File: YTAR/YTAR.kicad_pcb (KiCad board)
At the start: 6 copper layers, 50 x 50 mm, 148 parts, among them J1 STDC14, J2 CAMERA, J3 Micro_Sd, J5 USB_C_USB4085-GF-A, J6 IO, SW1 Tact, U1 STM32H750XBHx, U2 MCP2562-E-MF, U3 DS90C124, Y1 25MHz

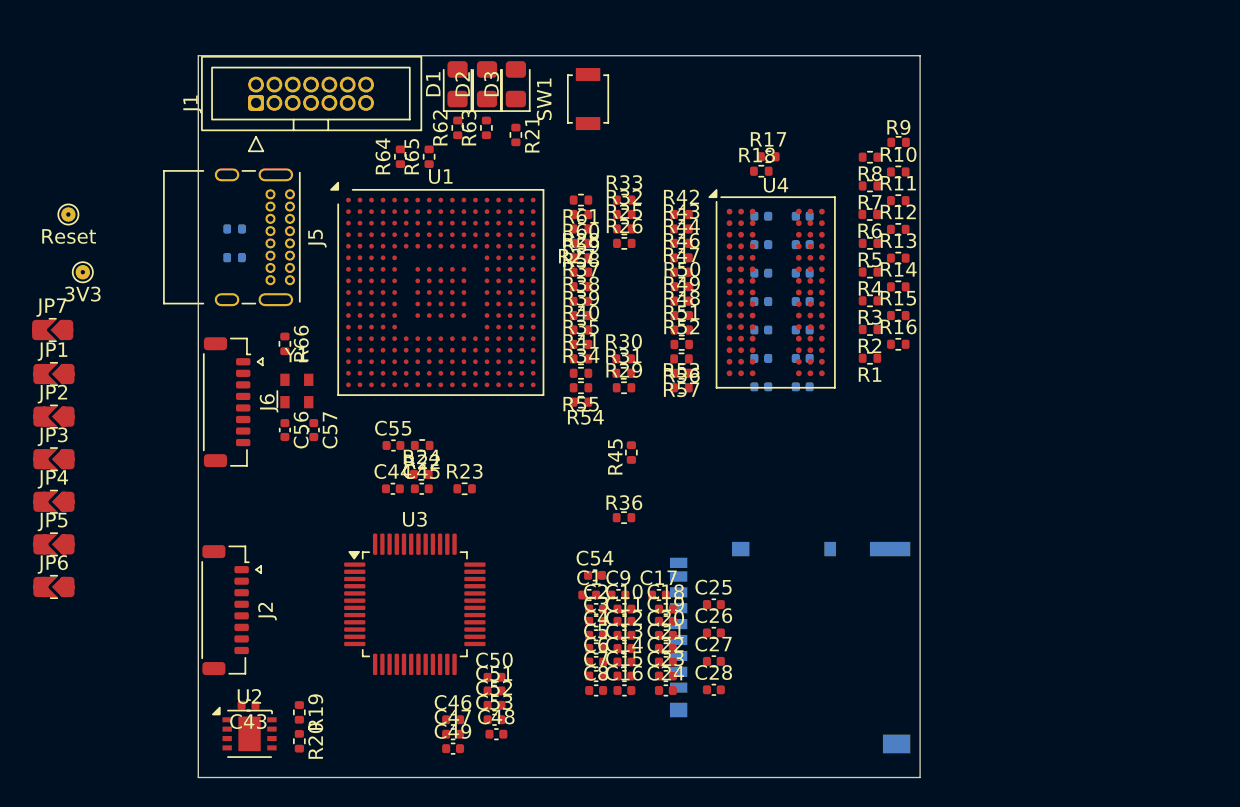
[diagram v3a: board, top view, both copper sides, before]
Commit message: Added LCD labels and corredted SRAM
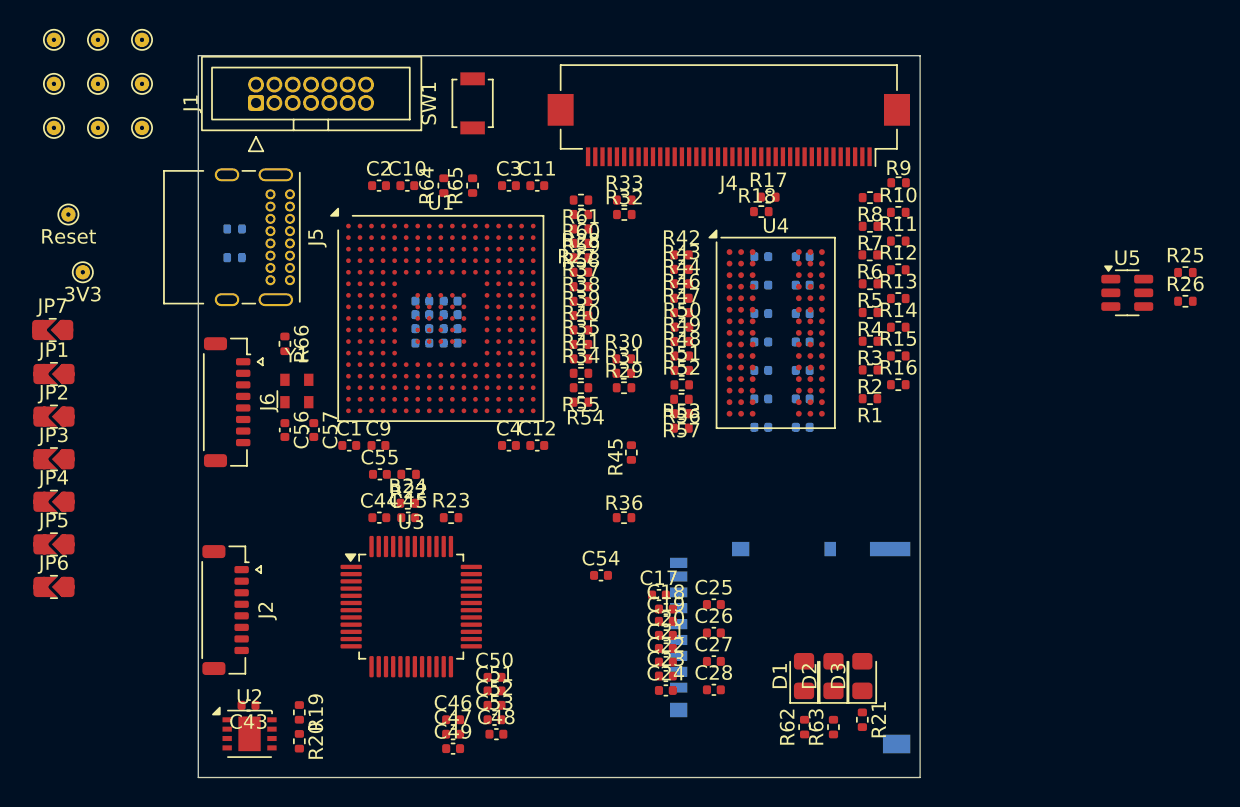
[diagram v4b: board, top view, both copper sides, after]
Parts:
- added J4: FH12-40S-0.5SH(55), Connector_FFC-FPC:Hirose_FH12-40S-0.5SH_1x40-1MP_P0.50mm_Horizontal, F.Cu at (48.8, 17.1)
- added TP10: ~, MEMS_Custom:TestPoint_Pad_D1.0mm, F.Cu at (8.10, 13.9)
- added TP11: ~, MEMS_Custom:TestPoint_Pad_D1.0mm, F.Cu at (8.10, 17.0)
- added TP3: ~, MEMS_Custom:TestPoint_Pad_D1.0mm, F.Cu at (2.00, 10.9)
- added TP4: ~, MEMS_Custom:TestPoint_Pad_D1.0mm, F.Cu at (2.00, 13.9)
- added TP5: ~, MEMS_Custom:TestPoint_Pad_D1.0mm, F.Cu at (2.00, 17.0)
- added TP6: ~, MEMS_Custom:TestPoint_Pad_D1.0mm, F.Cu at (5.05, 10.9)
- added TP7: ~, MEMS_Custom:TestPoint_Pad_D1.0mm, F.Cu at (5.05, 13.9)
- added TP8: ~, MEMS_Custom:TestPoint_Pad_D1.0mm, F.Cu at (5.05, 17.0)
- added TP9: ~, MEMS_Custom:TestPoint_Pad_D1.0mm, F.Cu at (8.10, 10.9)
- added U5: TPS56339, Package_TO_SOT_SMD:TSOT-23-6, F.Cu at (76.3, 28.4)
- C13, C14, C15, C16, C5, C6, C7, C8: moved to B.Cu
- moved R63 48.0 mm to (56.0, 58.5)
- moved R62 48.0 mm to (54.0, 58.5)
- moved D1 47.5 mm to (54.0, 55.0)
- moved D2 47.5 mm to (56.0, 55.0)
- moved D3 47.5 mm to (58.0, 55.0)
- moved R21 47.1 mm to (58.0, 58.0)
- moved R26 39.1 mm to (80.4, 29.0)
- moved R25 39.0 mm to (80.4, 27.0)
- moved C10 33.0 mm to (26.5, 21.0)
- moved C2 33.0 mm to (24.5, 21.0)
- moved C11 30.8 mm to (35.5, 21.0)
- moved C3 30.8 mm to (33.5, 21.0)
- moved C13 27.8 mm to (27.5, 29.0), turned to 180 degrees
- moved C14 27.8 mm to (27.5, 29.9), turned to 180 degrees
- moved C15 27.8 mm to (27.5, 30.9), turned to 180 degrees
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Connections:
- C10 pad 1: +3.3V -> VDDA
- C11 pad 1: +3.3V -> VDDA
- C12 pad 1: +3.3V -> VDDA
- C13 pad 1: +3.3V -> VDDA
- C14 pad 1: +3.3V -> VDDA
- C15 pad 1: +3.3V -> VDDA
- C16 pad 1: +3.3V -> VDDA
- C17 pad 1: +3.3V -> VDDA
- C18 pad 1: +3.3V -> VDDA
- C19 pad 1: +3.3V -> VDDA
- C20 pad 1: +3.3V -> VDDA
- C21 pad 1: +3.3V -> VDDA
- C22 pad 1: +3.3V -> VDDA
- C23 pad 1: +3.3V -> VDDA
- C24 pad 1: +3.3V -> VDDA
- C3 pad 1: +3.3V -> VDDA
- C4 pad 1: +3.3V -> VDDA
- C5 pad 1: +3.3V -> VDDA
- C6 pad 1: +3.3V -> VDDA
- C7 pad 1: +3.3V -> VDDA
- C8 pad 1: +3.3V -> VDDA
- C9 pad 1: +3.3V -> VDDA
- J6 pad 1: unconnected-(J6-Pin_1-Pad1) -> +12V_IN
- J6 pad 2: unconnected-(J6-Pin_2-Pad2) -> GND
- R25 pad 1: Net-(U1-PC14) -> Net-(U1-PD14)
- R26 pad 1: Net-(U1-PC15) -> Net-(U1-PD15)
- U1 pad A13: unconnected-(U1-PC10-PadA13) -> /ROUT10
- U1 pad A15: unconnected-(U1-PI1-PadA15) -> /LCD_G6
- U1 pad A16: unconnected-(U1-PI0-PadA16) -> /LCD_G5
- U1 pad A8: unconnected-(U1-PK5-PadA8) -> /LCD_B6
- U1 pad B10: unconnected-(U1-PJ15-PadB10) -> /LCD_B3
- U1 pad B13: unconnected-(U1-PC11-PadB13) -> /ROUT11
- U1 pad B8: unconnected-(U1-PK4-PadB8) -> /LCD_B5
- U1 pad C1: Net-(U1-PC15) -> /ROUT15
- U1 pad C12: unconnected-(U1-PC12-PadC12) -> /ROUT12
- U1 pad C2: Net-(U1-PC14) -> /ROUT14
- U1 pad C7: unconnected-(U1-PK6-PadC7) -> /LCD_B7
- U1 pad C8: unconnected-(U1-PK3-PadC8) -> /LCD_B4
- U1 pad D10: unconnected-(U1-PJ14-PadD10) -> /LCD_B2
- U1 pad D11: unconnected-(U1-PJ12-PadD11) -> /LCD_B0
- U1 pad D7: unconnected-(U1-PK7-PadD7) -> /LCD_DE
- U1 pad E10: unconnected-(U1-PJ13-PadE10) -> /LCD_B1
- U1 pad E13: unconnected-(U1-PC8-PadE13) -> /ROUT8
- U1 pad E14: unconnected-(U1-PC9-PadE14) -> /ROUT9
- U1 pad E2: unconnected-(U1-PI9-PadE2) -> /LCD_VSYNC
- U1 pad E3: unconnected-(U1-PC13-PadE3) -> /ROUT13
- U1 pad F13: unconnected-(U1-PC7-PadF13) -> /ROUT7
- U1 pad F14: unconnected-(U1-PC6-PadF14) -> /ROUT6
- U1 pad H1: unconnected-(U1-PI12-PadH1) -> /LCD_HSYNC
- U1 pad H17: unconnected-(U1-PK2-PadH17) -> /LCD_G7
- U1 pad H3: unconnected-(U1-PI14-PadH3) -> /LCD_CLK
- U1 pad K14: unconnected-(U1-PJ11-PadK14) -> /LCD_G4
- U1 pad L14: unconnected-(U1-PJ10-PadL14) -> /LCD_G3
- U1 pad L2: unconnected-(U1-PC0-PadL2) -> /ROUT0
- U1 pad M14: unconnected-(U1-PJ9-PadM14) -> /LCD_G2
- U1 pad M2: unconnected-(U1-PC1-PadM2) -> /ROUT1
- U1 pad M3: unconnected-(U1-PC2-PadM3) -> /ROUT2
- U1 pad M4: unconnected-(U1-PC3-PadM4) -> /ROUT3
- U1 pad N13: unconnected-(U1-PJ8-PadN13) -> /LCD_G1
- U1 pad N14: unconnected-(U1-PJ7-PadN14) -> /LCD_G0
- U1 pad N15: unconnected-(U1-PJ6-PadN15) -> /LCD_R7
- U1 pad N6: unconnected-(U1-PJ0-PadN6) -> /LCD_R1
- U1 pad P15: unconnected-(U1-PD15-PadP15) -> Net-(U1-PD15)
- U1 pad P16: unconnected-(U1-PD14-PadP16) -> Net-(U1-PD14)
- U1 pad P5: unconnected-(U1-PI15-PadP5) -> /LCD_R0
- U1 pad P6: unconnected-(U1-PJ1-PadP6) -> /LCD_R2
- U1 pad R12: unconnected-(U1-PJ5-PadR12) -> /LCD_R6
- U1 pad R13: unconnected-(U1-PH9-PadR13) -> /LCD_R3
- U1 pad R16: unconnected-(U1-PD12-PadR16) -> /LCD_SCL
- U1 pad R17: unconnected-(U1-PD13-PadR17) -> /LCD_SDA
- U1 pad T4: unconnected-(U1-PC4-PadT4) -> /ROUT4
- U1 pad U4: unconnected-(U1-PC5-PadU4) -> /ROUT5
- U1 pad U6: unconnected-(U1-PJ3-PadU6) -> /LCD_R4
- U1 pad U7: unconnected-(U1-PJ4-PadU7) -> /LCD_R5

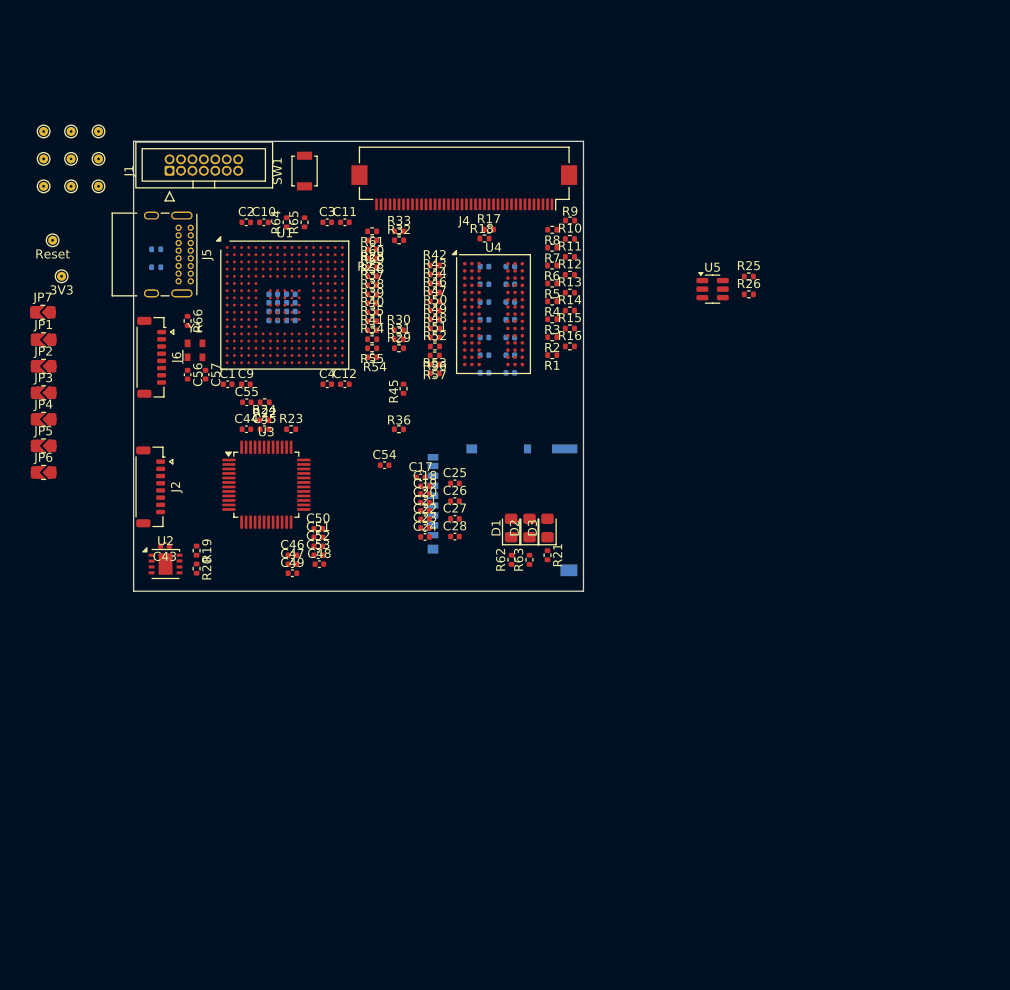
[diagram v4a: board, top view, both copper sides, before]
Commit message: Started a bit of routing
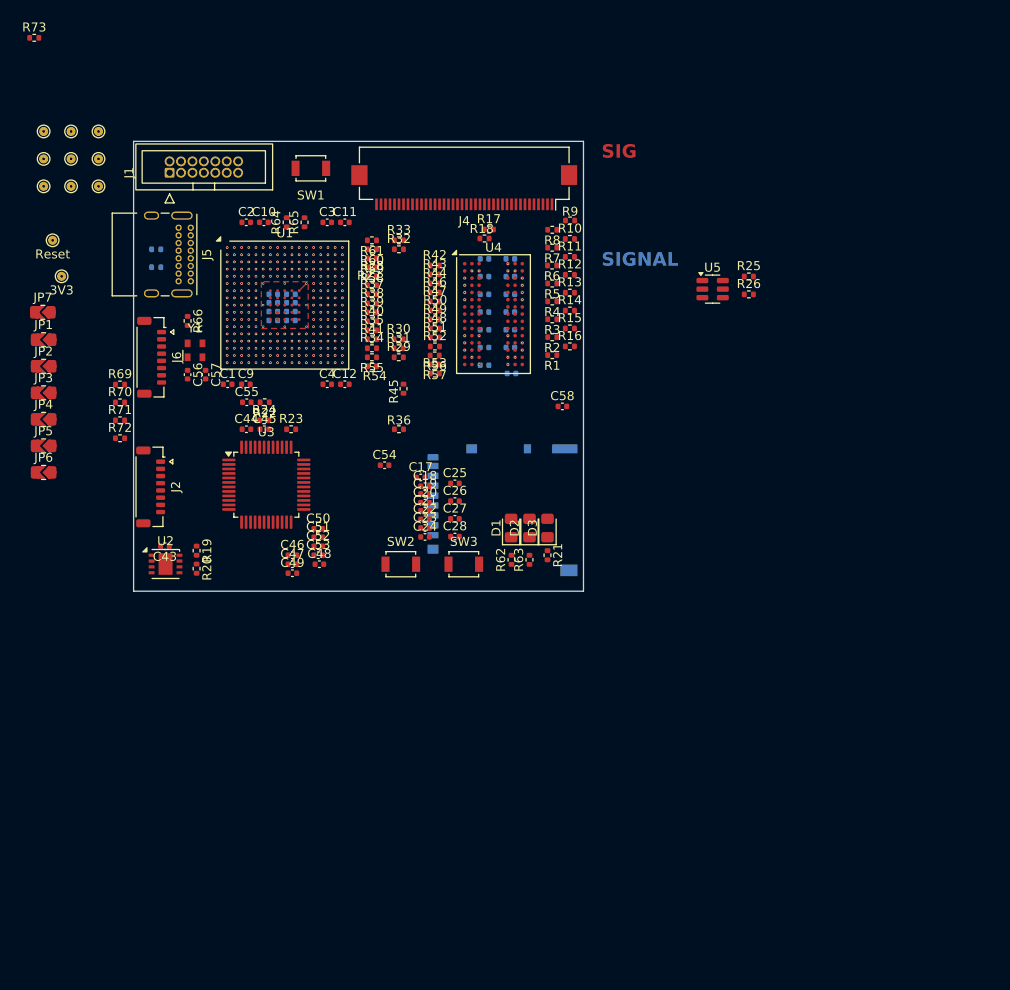
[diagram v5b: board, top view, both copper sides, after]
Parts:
- added C58: 2.2u, Capacitor_SMD:C_0402_1005Metric, F.Cu at (59.7, 41.5)
- added R69: 10k, Resistor_SMD:R_0402_1005Metric, F.Cu at (10.5, 39.0)
- added R70: 10k, Resistor_SMD:R_0402_1005Metric, F.Cu at (10.5, 41.0)
- added R71: 5k1, Resistor_SMD:R_0402_1005Metric, F.Cu at (10.5, 43.0)
- added R72: 5k1, Resistor_SMD:R_0402_1005Metric, F.Cu at (10.5, 45.0)
- added R73: 0R, Resistor_SMD:R_0402_1005Metric, F.Cu at (0.95, 0.49)
- added SW2: PICTURE, Button_Switch_SMD:SW_SPST_B3U-1000P, F.Cu at (41.7, 59.0)
- added SW3: MODE, Button_Switch_SMD:SW_SPST_B3U-1000P, F.Cu at (48.7, 59.0)
- SW1: value Tact -> RESET
- moved R29 1.00 mm to (41.5, 36.0)
- moved R27 1.00 mm to (38.5, 28.0)
- moved R28 1.00 mm to (38.5, 27.0)
- moved R30 1.00 mm to (41.5, 34.0)
- moved R31 1.00 mm to (41.5, 35.0)
- moved R32 1.00 mm to (41.5, 24.0)
- moved R33 1.00 mm to (41.5, 23.0)
- moved R34 1.00 mm to (38.5, 35.0)
- moved R35 1.00 mm to (38.5, 33.0)
- moved R37 1.00 mm to (38.5, 29.0)
- moved R38 1.00 mm to (38.5, 30.0)
- moved R39 1.00 mm to (38.5, 31.0)
- moved R40 1.00 mm to (38.5, 32.0)
- moved R41 1.00 mm to (38.5, 34.0)
- moved R54 1.00 mm to (38.5, 37.0)
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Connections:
- C10 pad 1: VDDA -> VDD_MCU
- C11 pad 1: VDDA -> VDD_MCU
- C12 pad 1: VDDA -> VDD_MCU
- C13 pad 1: VDDA -> VDD_MCU
- C14 pad 1: VDDA -> VDD_MCU
- C15 pad 1: VDDA -> VDD_MCU
- C16 pad 1: VDDA -> VDD_MCU
- C17 pad 1: VDDA -> VDD_MCU
- C18 pad 1: VDDA -> VDD_MCU
- C19 pad 1: VDDA -> VDD_MCU
- C20 pad 1: VDDA -> VDD_MCU
- C21 pad 1: VDDA -> VDD_MCU
- C22 pad 1: VDDA -> VDD_MCU
- C23 pad 1: VDDA -> VDD_MCU
- C24 pad 1: VDDA -> VDD_MCU
- C25 pad 1: VDDA -> VDD_MCU
- C26 pad 1: VDDA -> VDD_MCU
- C27 pad 1: VDDA -> VDD_MCU
- C3 pad 1: VDDA -> VDD_MCU
- C4 pad 1: VDDA -> VDD_MCU
- C5 pad 1: VDDA -> VDD_MCU
- C54 pad 1: VDDA -> VDD_MCU
- C6 pad 1: VDDA -> VDD_MCU
- C7 pad 1: VDDA -> VDD_MCU
- C8 pad 1: VDDA -> VDD_MCU
- C9 pad 1: VDDA -> VDD_MCU
- J1 pad 3: VDDA -> VDD_MCU
- J3 pad 1: unconnected-(J3-DAT2-Pad1) -> /SD_D2
- J3 pad 10: unconnected-(J3-DET_A-Pad10) -> /SD_DET_A
- J3 pad 11: unconnected-(J3-SHIELD-Pad11) -> GND
- J3 pad 2: unconnected-(J3-DAT3/CD-Pad2) -> /SD_D3
- J3 pad 3: unconnected-(J3-CMD-Pad3) -> /SD_CMD
- J3 pad 4: unconnected-(J3-VDD-Pad4) -> VDD_MCU
- J3 pad 5: unconnected-(J3-CLK-Pad5) -> /SD_CK
- J3 pad 6: unconnected-(J3-VSS-Pad6) -> GND
- J3 pad 7: unconnected-(J3-DAT0-Pad7) -> /SD_D0
- J3 pad 8: unconnected-(J3-DAT1-Pad8) -> /SD_D1
- J3 pad 9: unconnected-(J3-DET_B-Pad9) -> GND
- J6 pad 3: unconnected-(J6-Pin_3-Pad3) -> /I2C2_SCL
- J6 pad 4: unconnected-(J6-Pin_4-Pad4) -> /I2C2_SDA
- J6 pad MP: unconnected-(J6-PadMP) -> GND
- JP1 pad 2: VDDA -> VDD_MCU
- JP7 pad 2: VDDA -> VDD_MCU
- R62 pad 2: unconnected-(R62-Pad2) -> /LED_GREEN
- R63 pad 2: unconnected-(R63-Pad2) -> /LED_ORANGE
- R64 pad 2: VDDA -> VDD_MCU
- U1 pad A6: VDDA -> VDD_MCU
- U1 pad B1: VDDA -> VDD_MCU
- U1 pad B11: unconnected-(U1-PD6-PadB11) -> /SD_CK
- U1 pad B7: unconnected-(U1-PB4-PadB7) -> /SD_D3
- U1 pad B9: unconnected-(U1-PG11-PadB9) -> /SD_D2
- U1 pad C11: unconnected-(U1-PD7-PadC11) -> /SD_CMD
- U1 pad C17: VDDA -> VDD_MCU
- U1 pad E11: VDDA -> VDD_MCU
- U1 pad E6: VDDA -> VDD_MCU
- U1 pad E9: VDDA -> VDD_MCU
- U1 pad F17: VDDA -> VDD_MCU
- U1 pad F5: VDDA -> VDD_MCU
- U1 pad G13: VDDA -> VDD_MCU
- U1 pad G17: VDDA -> VDD_MCU
- U1 pad G5: VDDA -> VDD_MCU
- U1 pad H13: VDDA -> VDD_MCU
- U1 pad H5: VDDA -> VDD_MCU
- U1 pad J13: VDDA -> VDD_MCU
- U1 pad K13: VDDA -> VDD_MCU
- U1 pad K5: VDDA -> VDD_MCU
- U1 pad L13: VDDA -> VDD_MCU
- U1 pad L5: VDDA -> VDD_MCU
- U1 pad M13: VDDA -> VDD_MCU
- U1 pad M5: VDDA -> VDD_MCU
- U1 pad N10: VDDA -> VDD_MCU
- U1 pad N11: VDDA -> VDD_MCU
- U1 pad N12: VDDA -> VDD_MCU
- U1 pad N4: unconnected-(U1-PA1-PadN4) -> /DES_LOCK
- U1 pad N5: unconnected-(U1-PA0-PadN5) -> /DES_RCLK
- U1 pad N7: VDDA -> VDD_MCU
- U1 pad N8: VDDA -> VDD_MCU
- U1 pad P11: unconnected-(U1-PB10-PadP11) -> /I2C2_SCL
- U1 pad P12: unconnected-(U1-PB11-PadP12) -> /I2C2_SDA
- U1 pad P17: VDDA -> VDD_MCU
- U1 pad T15: unconnected-(U1-PB15-PadT15) -> /SD_D1
- U1 pad U12: VDDA -> VDD_MCU
- U1 pad U15: unconnected-(U1-PB14-PadU15) -> /SD_D0
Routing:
- net GND: track 0.00 -> 1.13 mm, vias 0 -> 44
- net unconnected-(U1-PK1-PadJ15): vias 0 -> 1
- net unconnected-(U1-PK0-PadJ14): vias 0 -> 1
- net unconnected-(U1-PJ2-PadT6): vias 0 -> 1
- net unconnected-(U1-PI8-PadE4): vias 0 -> 1
- net unconnected-(U1-PI7-PadB3): vias 0 -> 1
- net unconnected-(U1-PI6-PadA2): vias 0 -> 1
- net unconnected-(U1-PI5-PadA3): vias 0 -> 1
- net unconnected-(U1-PI4-PadA4): vias 0 -> 1
- net unconnected-(U1-PI3-PadC14): vias 0 -> 1
- net unconnected-(U1-PI2-PadB15): vias 0 -> 1
- net unconnected-(U1-PI13-PadH2): vias 0 -> 1
- net unconnected-(U1-PI11-PadF4): vias 0 -> 1
- net unconnected-(U1-PI10-PadF3): vias 0 -> 1
- net unconnected-(U1-PH8-PadT13): vias 0 -> 1
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- added copper zone on F.Cu, net GND
- added copper zone on In4.Cu, net VDD_MCU
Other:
- board text added: "GND"
- board text added: "PWR"
- board text added: "SIG"
- board text added: "SIGNAL"
